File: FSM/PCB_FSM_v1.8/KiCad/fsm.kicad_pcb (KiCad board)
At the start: 2 copper layers, 27 parts

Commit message: KiCad final
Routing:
- net B0: track 50.6 -> 59.2 mm
- net GND: track 23.4 -> 22.8 mm

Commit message: Pega bruno
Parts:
- added B1: SW_Push, Button_Switch_THT:SW_PUSH_6mm_H7.3mm, F.Cu at (58.4, 87.6)
- added BRST1: Conn_01x02_Female, Connector_PinSocket_1.00mm:PinSocket_1x02_P1.00mm_Vertical, F.Cu at (67.9, 85.1)
- added BRST2: SW_Push, Button_Switch_THT:SW_PUSH_6mm_H7.3mm, F.Cu at (78.1, 86.4)
- added RRST1: 100k, Resistor_THT:R_Axial_DIN0207_L6.3mm_D2.5mm_P7.62mm_Horizontal, F.Cu at (71.1, 78.1)
- CButt1: renamed from C10; footprint Capacitor_THT:C_Disc_D3.0mm_W2.0mm_P2.50mm -> Capacitor_THT:CP_Radial_D4.0mm_P1.50mm
- R3: value 6,2k -> 10k
- R4: value 6,2k -> 1k
- moved RRST2 40.9 mm to (71.1, 74.3)
- moved CRST1 40.0 mm to (82.5, 78.1), turned to 270 degrees
- moved C7 24.7 mm to (85.7, 81.9), turned to 270 degrees
- moved SCHMITT1 23.7 mm to (88.3, 87.0)
- moved AND1 12.8 mm to (61.0, 57.1)
- moved C9 12.7 mm to (56.5, 62.2)
- moved FFJK1 12.7 mm to (60.3, 69.8)
- moved R3 12.5 mm to (63.5, 74.3), turned to 180 degrees
- moved CButt1 9.09 mm to (63.5, 86.4), turned to 90 degrees
- moved C5 5.12 mm to (56.5, 54.6)
- moved R4 5.12 mm to (55.9, 78.1), turned to 0 degrees
- renumbered Alimentações to Alimentações1, Botão to Botão1, CRST to CRST1, FFJK to FFJK1, NOT to NOT1, RRST to RRST2, SCHMITT to SCHMITT1, Saídas to Saídas1, Sensores to Sensores1
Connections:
- AND1 pad 10: B0 -> Net-(AND1-Pad10)
- AND1 pad 14: +5V -> (no net)
- AND1 pad 5: Net-(AND1-Pad3) -> B0
- AND1 pad 6: B0 -> Net-(AND1-Pad3)
- AND1 pad 7: GND -> (no net)
- AND1 pad 8: Net-(AND1-Pad10) -> B0
- AND4 pad 14: +5V -> (no net)
- AND4 pad 7: GND -> (no net)
- FFJK1 pad 16: +5V -> (no net)
- FFJK1 pad 8: GND -> (no net)
- NOT1 pad 14: +5V -> (no net)
- NOT1 pad 7: GND -> (no net)
- OR1 pad 10: BWL -> FWR
- OR1 pad 14: +5V -> (no net)
- OR1 pad 7: GND -> (no net)
- OR1 pad 8: FWR -> BWL
- RRST2 pad 1: +5V -> Net-(BRST1-Pad1)
- SCHMITT1 pad 1: +5V -> (no net)
- SCHMITT1 pad 10: B0 -> (no net)
- SCHMITT1 pad 14: +5V -> (no net)
- SCHMITT1 pad 3: (no net) -> GND
- SCHMITT1 pad 4: (no net) -> B
- SCHMITT1 pad 5: (no net) -> +5V
- SCHMITT1 pad 7: GND -> (no net)
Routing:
- net S5: track 97.3 -> 12.4 mm, vias 1 -> 0
- net B0: track 59.2 -> 2.43 mm
- net Net-(FFJK1-Pad2): track 45.2 -> 1.80 mm, vias 1 -> 0
- net Net-(AND1-Pad3): track 50.6 -> 7.18 mm
- net FWL: track 49.6 -> 6.55 mm
- net Net-(AND1-Pad4): track 38.7 -> 0.00 mm, vias 1 -> 0
- net +5V: track 50.9 -> 16.8 mm, vias 1 -> 0
- net Net-(FFJK1-Pad3): track 34.9 -> 1.80 mm
- net B1': track 34.9 -> 9.42 mm
- net BWL: track 56.9 -> 31.7 mm
- net Net-(BRST1-Pad1): track 0.00 -> 24.7 mm
- net Net-(CButt1-Pad2): track 12.5 -> 36.0 mm
- net GND: track 22.8 -> 0.00 mm
- net S8: track 24.5 -> 3.81 mm
- net B_IN: track 11.4 -> 29.0 mm
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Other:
- board text added: "AWR-19 Analog Waiter Robot"

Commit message: KiCad over
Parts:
- BRST1: footprint Connector_PinSocket_1.00mm:PinSocket_1x02_P1.00mm_Vertical -> Connector_PinSocket_2.00mm:PinSocket_1x02_P2.00mm_Vertical
- moved C8 31.8 mm to (85.7, 68.6), turned to 90 degrees
- moved C3 31.5 mm to (57.8, 37.5)
- moved NOT1 26.7 mm to (88.9, 71.1)
- moved OR1 26.7 mm to (88.9, 43.2)
- moved R1 25.6 mm to (75.6, 43.2), turned to 90 degrees
- moved C4 24.1 mm to (85.7, 38.1), turned to 270 degrees
- moved R2 16.7 mm to (78.7, 35.6), turned to 270 degrees
- moved C6 13.5 mm to (85.7, 54.6)
- moved C1 10.8 mm to (81.9, 38.1), turned to 270 degrees
- moved C2 4.62 mm to (72.4, 40.6)
- moved NE555 4.26 mm to (61.0, 42.5)
- moved C9 3.86 mm to (57.1, 66.0)
- moved BRST2 2.62 mm to (78.7, 88.9)
- moved R3 2.62 mm to (64.1, 76.8)
- moved R4 2.62 mm to (56.5, 80.6)
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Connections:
- AND1 pad 14: (no net) -> +5V
- AND1 pad 7: (no net) -> GND
- AND4 pad 14: (no net) -> +5V
- AND4 pad 7: (no net) -> GND
- FFJK1 pad 16: (no net) -> +5V
- FFJK1 pad 8: (no net) -> GND
- NOT1 pad 14: (no net) -> +5V
- NOT1 pad 7: (no net) -> GND
- OR1 pad 14: (no net) -> +5V
- OR1 pad 7: (no net) -> GND
- SCHMITT1 pad 14: (no net) -> +5V
- SCHMITT1 pad 7: (no net) -> GND
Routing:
- net +5V: track 16.8 -> 196.8 mm
- net B0: track 2.43 -> 71.6 mm
- net S5: track 12.4 -> 72.1 mm
- net Net-(FFJK1-Pad3): track 1.80 -> 53.6 mm
- net B1': track 9.42 -> 60.9 mm
- net Net-(AND1-Pad3): track 7.18 -> 55.7 mm
- net Net-(FFJK1-Pad2): track 1.80 -> 47.8 mm, vias 0 -> 1
- net FWL: track 6.55 -> 51.7 mm
- net B: track 0.00 -> 34.6 mm
- net BWL: track 31.7 -> 64.0 mm
- net CLK: track 2.54 -> 33.3 mm
- net Net-(AND4-Pad4): track 6.13 -> 34.2 mm
- net Net-(AND4-Pad3): track 6.13 -> 28.0 mm
- net Net-(AND4-Pad10): track 29.2 -> 10.4 mm
- net FWR: track 11.7 -> 29.3 mm
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- added copper zone on F.Cu, net GND
- removed copper zone on F.Cu, net +5V
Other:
- board text added: "AWR-19_PCB_FSM"
- board text removed: "AWR-19 Analog Waiter Robot"

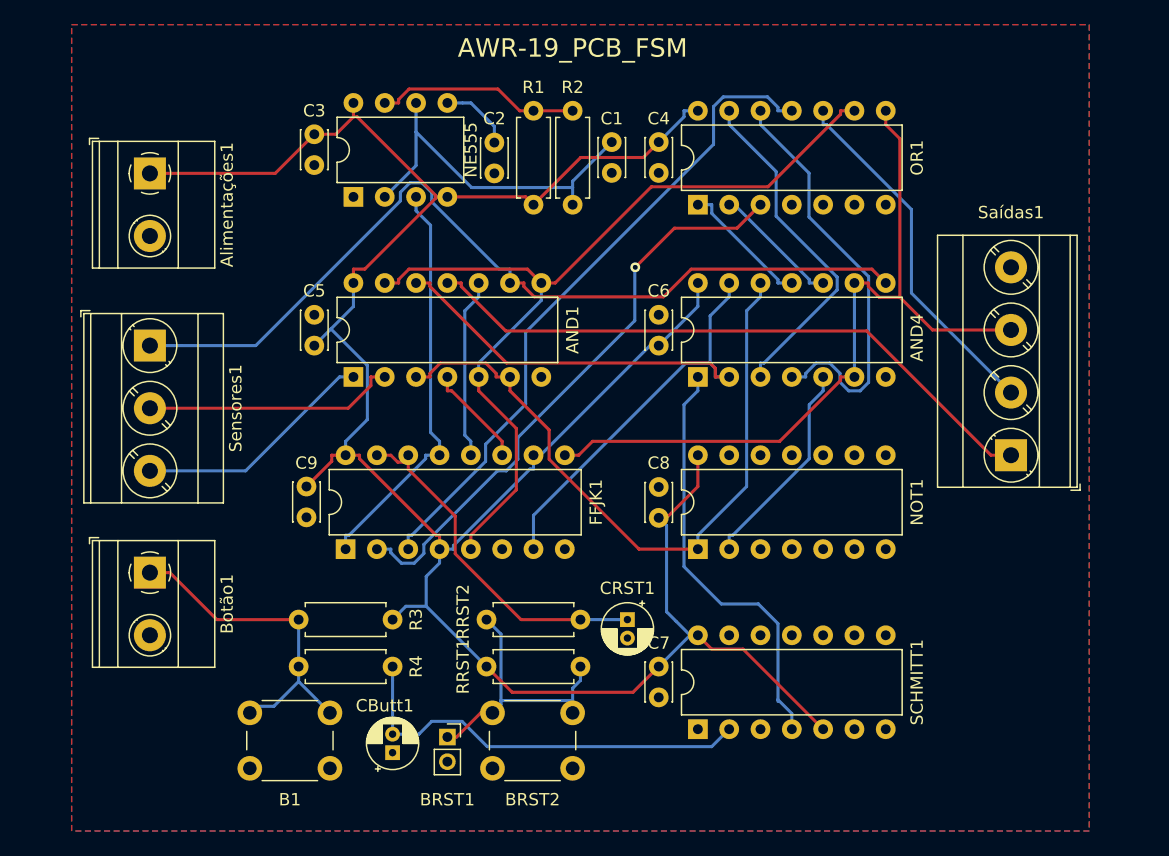
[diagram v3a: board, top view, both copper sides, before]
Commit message: alteration in 3D view
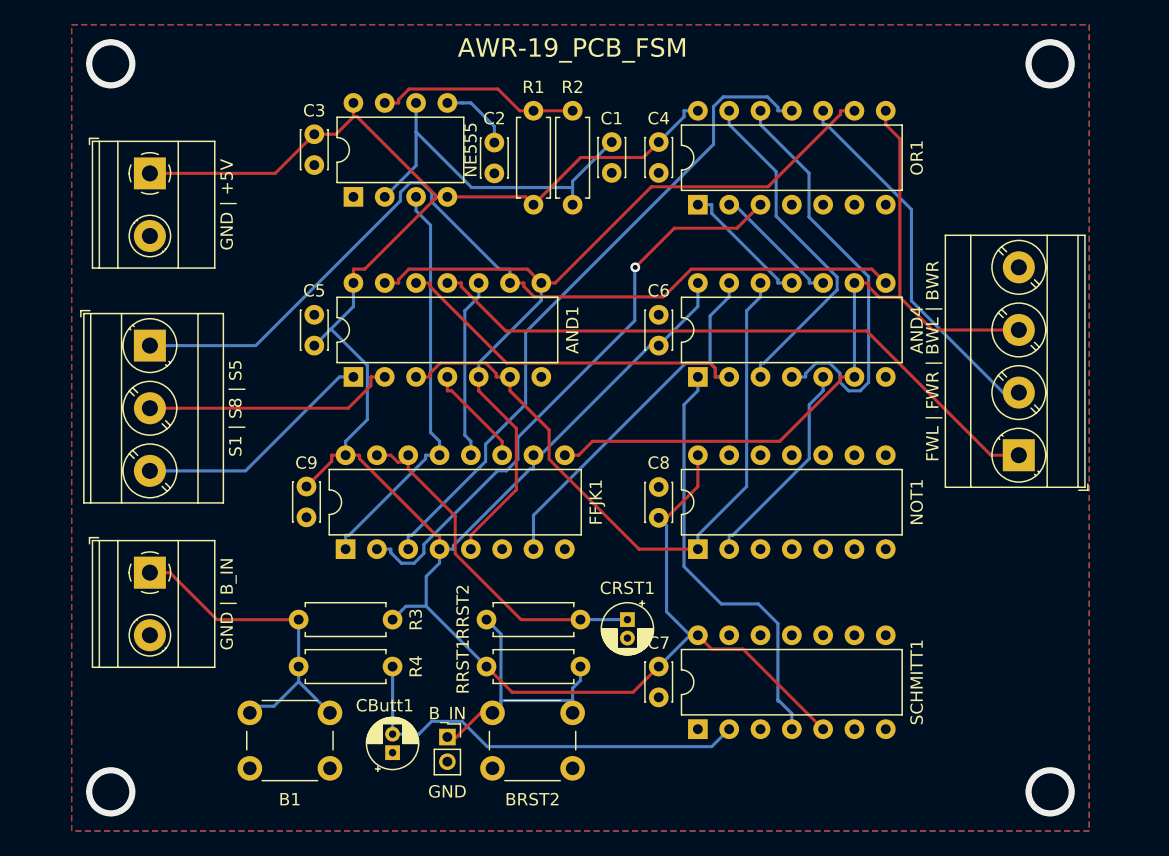
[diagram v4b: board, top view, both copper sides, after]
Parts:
- FWL | FWR | BWL | BWR: renamed from Saídas1
- GND | +5V: renamed from Alimentações1
- GND | B_IN: renamed from Botão1
- S1 | S8 | S5: renamed from Sensores1
- moved FWL | FWR | BWL | BWR 0.64 mm to (114.9, 63.5)
- renumbered BRST1 to GND
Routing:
- net FWR: track 29.3 -> 30.3 mm
- net FWL: track 51.7 -> 52.3 mm
- net BWL: track 64.0 -> 64.6 mm
- net (no net): vias 0 -> 4
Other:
- board text added: "B_IN"

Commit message: alteration in 3D view
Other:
- board text added: "AWR-19_FSM"
- board text removed: "AWR-19_PCB_FSM"
